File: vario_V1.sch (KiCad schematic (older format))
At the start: 34 parts, among them J1 Conn_01x02_Male, J2 Conn_ARM_JTAG_SWD_10, J3 Conn_01x02_Male, Q1 MMBT3904, SW1 SW_DIP_x01, U1 TPS61221DCK, U2 STM32F042F6Px, U3 PCF8551ATT_AJ, U4 LPS25HB, U5 LCD-S401C52TR

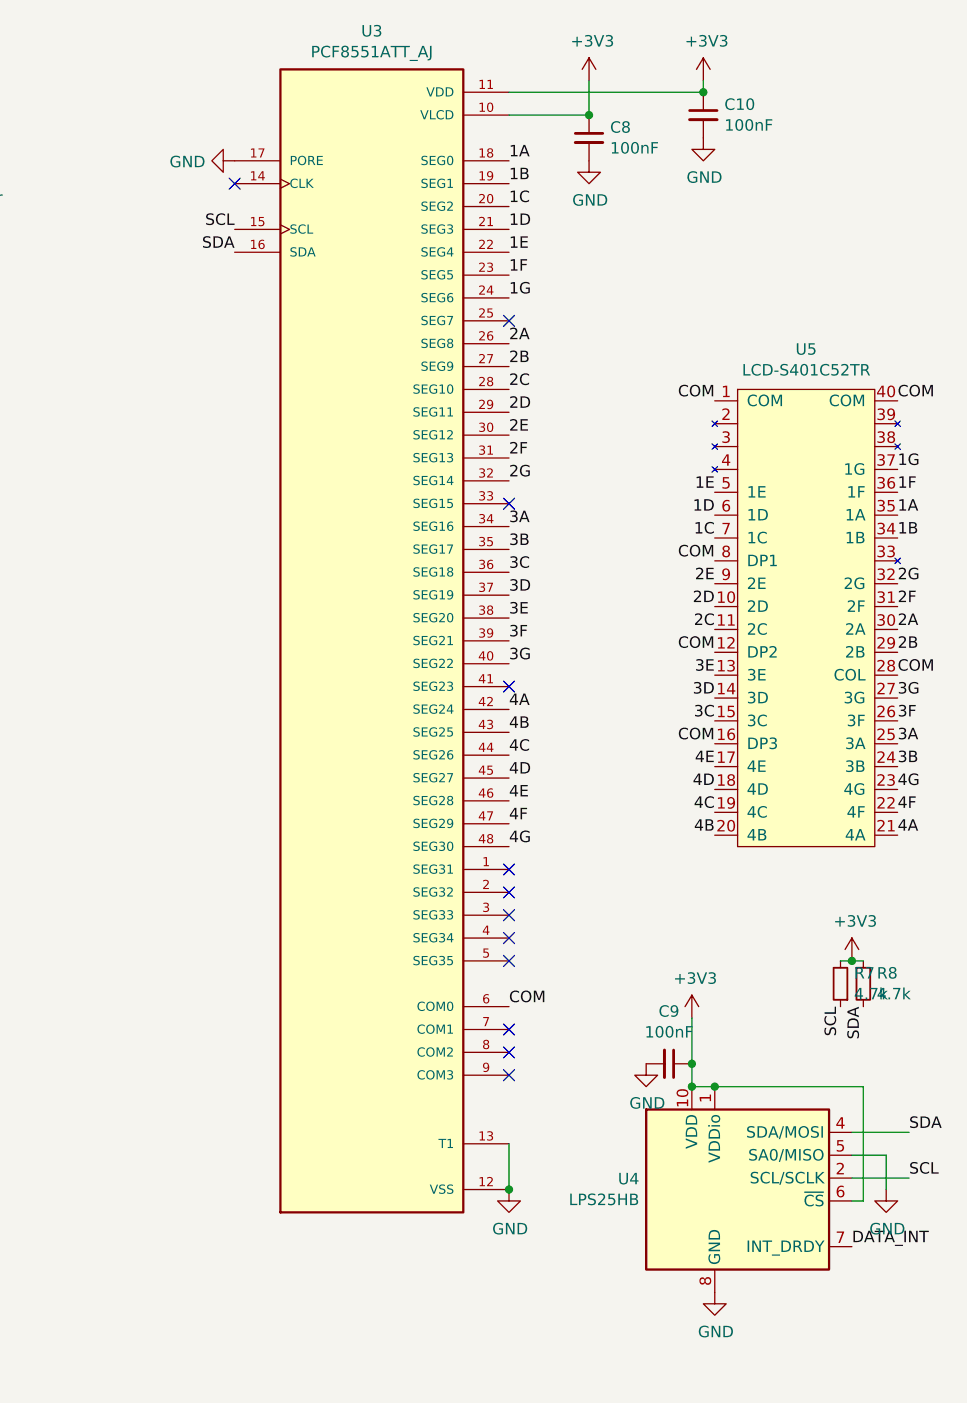
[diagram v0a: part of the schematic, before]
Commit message: Removing LCD
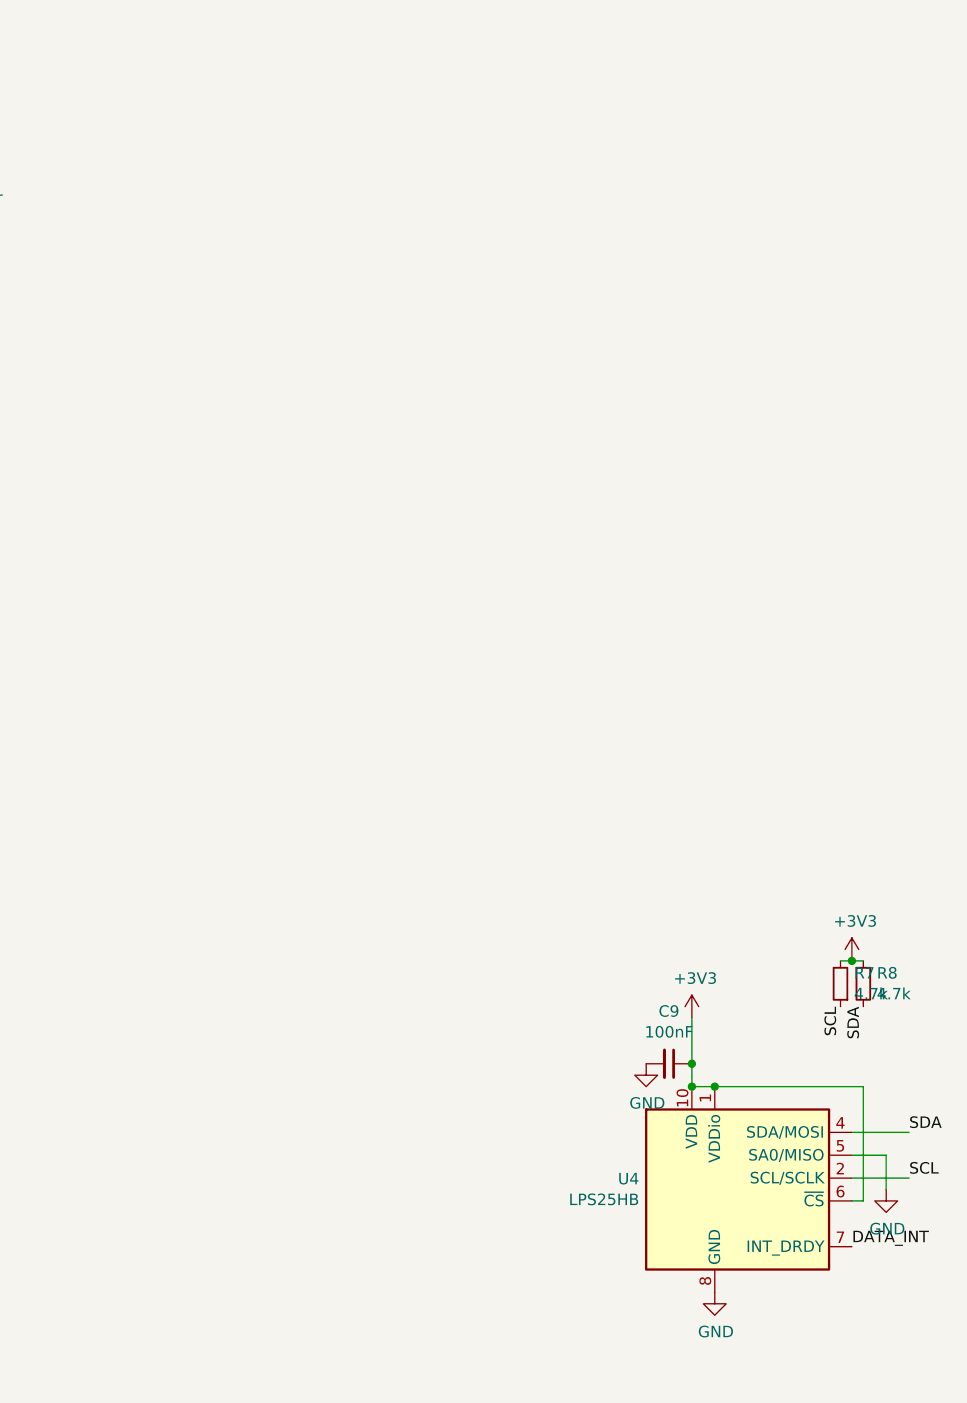
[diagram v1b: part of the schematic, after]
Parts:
- removed C10, C8: 100nF, Capacitor_SMD:C_0402_1005Metric, symbol Device:C_Small
- removed U3: PCF8551ATT_AJ, SOP50P810X120-48N, symbol lcd_decoder:PCF8551ATT_AJ
- removed U5: LCD-S401C52TR, vario:DIP-40_W32.4mm_Socket, symbol vario:LCD-S401C52TR
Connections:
- no-connect marks 22 -> 10
